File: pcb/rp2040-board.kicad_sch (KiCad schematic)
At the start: 61 parts, among them J1 DMX, J2 GPIO, J3 ELRS, J4 OLED, J5 SWD, J6 USB_C_Receptacle_USB2.0_16P, J7 AUDIO, SW1 TS-1187A-B-A-B, SW2 RotaryEncoder_Switch, SW3 TS-1187A-B-A-B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

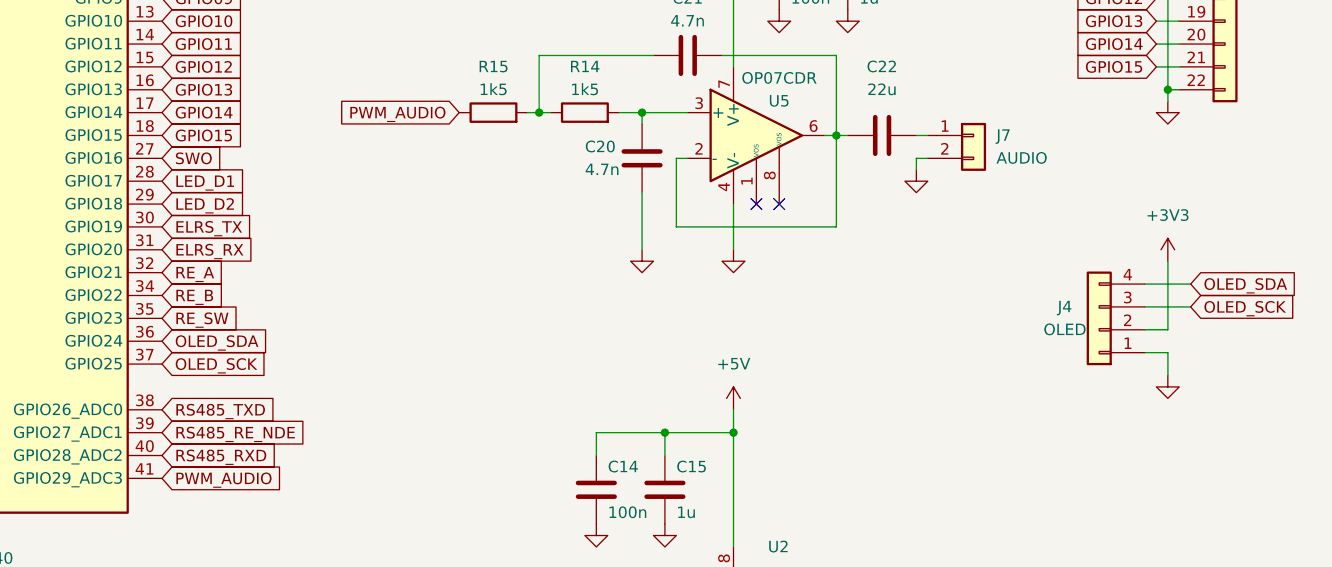
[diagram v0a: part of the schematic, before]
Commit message: fixed pin assignment issues
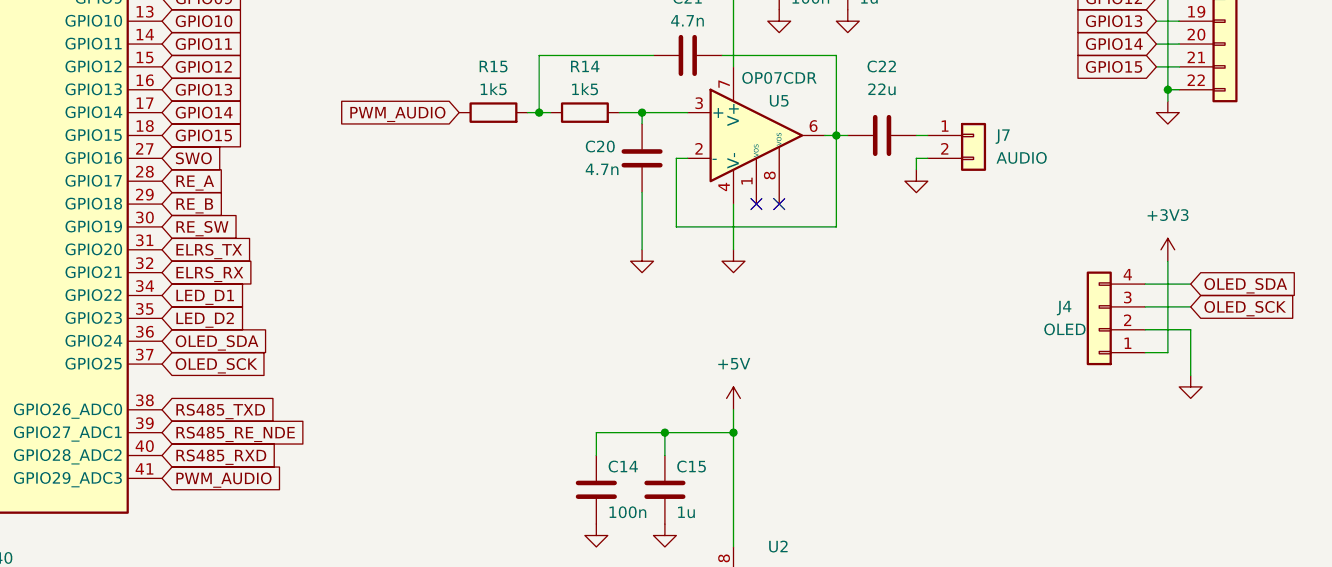
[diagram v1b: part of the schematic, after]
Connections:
- net +3V3: now also J4.1 (Pin_1); no longer J4.2 (Pin_2)
- net ELRS_RX: now also U3.32 (GPIO21); no longer U3.31 (GPIO20)
- net ELRS_TX: now also U3.31 (GPIO20); no longer U3.30 (GPIO19)
- net GND: now also J4.2 (Pin_2); no longer J4.1 (Pin_1)
- net LED_D1: now also U3.34 (GPIO22); no longer U3.28 (GPIO17)
- net LED_D2: now also U3.35 (GPIO23); no longer U3.29 (GPIO18)
- net RE_A: now also U3.28 (GPIO17); no longer U3.32 (GPIO21)
- net RE_B: now also U3.29 (GPIO18); no longer U3.34 (GPIO22)
- net RE_SW: now also U3.30 (GPIO19); no longer U3.35 (GPIO23)
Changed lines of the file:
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@@
   (no_connect (at 46.99 105.41))
   (no_connect (at 223.52 92.71))
+  (wire (pts (xy 266.7 109.22) (xy 264.16 109.22))
+    (stroke (width 0) (type default))
+  )
   (wire (pts (xy 106.68 181.61) (xy 105.41 181.61))
     (stroke (width 0) (type default))
@@
     (stroke (width 0) (type default))
   )
-  (wire (pts (xy 266.7 111.76) (xy 266.7 109.22))
-    (stroke (width 0) (type default))
-  )
   (wire (pts (xy 105.41 189.23) (xy 114.3 189.23))
     (stroke (width 0) (type default))
@@
     (stroke (width 0) (type default))
   )
+  (wire (pts (xy 269.24 106.68) (xy 269.24 111.76))
+    (stroke (width 0) (type default))
+  )
   (wire (pts (xy 49.53 162.56) (xy 50.8 162.56))
     (stroke (width 0) (type default))
@@
     (stroke (width 0) (type default))
   )
+  (wire (pts (xy 264.16 106.68) (xy 269.24 106.68))
+    (stroke (width 0) (type default))
+  )
   (wire (pts (xy 259.08 157.48) (xy 259.08 158.75))
     (stroke (width 0) (type default))
@@
     (stroke (width 0) (type default))
   )
-  (wire (pts (xy 264.16 106.68) (xy 266.7 106.68))
-    (stroke (width 0) (type default))
-  )
   (wire (pts (xy 265.43 54.61) (xy 267.97 54.61))
     (stroke (width 0) (type default))
@@
     (stroke (width 0) (type default))
   )
-  (wire (pts (xy 266.7 106.68) (xy 266.7 99.06))
+  (wire (pts (xy 266.7 99.06) (xy 266.7 109.22))
     (stroke (width 0) (type default))
   )
@@
   )
   (wire (pts (xy 64.77 27.94) (xy 72.39 27.94))
-    (stroke (width 0) (type default))
-  )
-  (wire (pts (xy 264.16 109.22) (xy 266.7 109.22))
     (stroke (width 0) (type default))
   )
@@
     )
   )
-  (global_label "RE_B" (shape input) (at 154.94 102.87 0) (fields_autoplaced)
-    (effects (font (size 1.27 1.27)) (justify left))
-    (property "Intersheetrefs" "${INTERSHEET_REFS}" (at 162.5818 102.87 0)
+  (global_label "RE_B" (shape input) (at 154.94 92.71 0) (fields_autoplaced)
+    (effects (font (size 1.27 1.27)) (justify left))
+    (property "Intersheetrefs" "${INTERSHEET_REFS}" (at 162.5818 92.71 0)
       (effects (font (size 1.27 1.27)) (justify left) hide)
     )
@@
     )
   )
-  (global_label "LED_D1" (shape input) (at 154.94 90.17 0) (fields_autoplaced)
-    (effects (font (size 1.27 1.27)) (justify left))
-    (property "Intersheetrefs" "${INTERSHEET_REFS}" (at 164.8194 90.17 0)
+  (global_label "LED_D1" (shape input) (at 154.94 102.87 0) (fields_autoplaced)
+    (effects (font (size 1.27 1.27)) (justify left))
+    (property "Intersheetrefs" "${INTERSHEET_REFS}" (at 164.8194 102.87 0)
       (effects (font (size 1.27 1.27)) (justify left) hide)
     )
@@
     )
   )
-  (global_label "ELRS_RX" (shape input) (at 154.94 97.79 0) (fields_autoplaced)
-    (effects (font (size 1.27 1.27)) (justify left))
-    (property "Intersheetrefs" "${INTERSHEET_REFS}" (at 166.0289 97.79 0)
+  (global_label "ELRS_RX" (shape input) (at 154.94 100.33 0) (fields_autoplaced)
+    (effects (font (size 1.27 1.27)) (justify left))
+    (property "Intersheetrefs" "${INTERSHEET_REFS}" (at 166.0289 100.33 0)
       (effects (font (size 1.27 1.27)) (justify left) hide)
     )
@@
     )
   )
-  (global_label "RE_SW" (shape input) (at 154.94 105.41 0) (fields_autoplaced)
-    (effects (font (size 1.27 1.27)) (justify left))
-    (property "Intersheetrefs" "${INTERSHEET_REFS}" (at 163.9727 105.41 0)
+  (global_label "RE_SW" (shape input) (at 154.94 95.25 0) (fields_autoplaced)
+    (effects (font (size 1.27 1.27)) (justify left))
+    (property "Intersheetrefs" "${INTERSHEET_REFS}" (at 163.9727 95.25 0)
       (effects (font (size 1.27 1.27)) (justify left) hide)
     )
@@
     )
   )
-  (global_label "ELRS_TX" (shape input) (at 154.94 95.25 0) (fields_autoplaced)
-    (effects (font (size 1.27 1.27)) (justify left))
-    (property "Intersheetrefs" "${INTERSHEET_REFS}" (at 165.7265 95.25 0)
+  (global_label "ELRS_TX" (shape input) (at 154.94 97.79 0) (fields_autoplaced)
+    (effects (font (size 1.27 1.27)) (justify left))
+    (property "Intersheetrefs" "${INTERSHEET_REFS}" (at 165.7265 97.79 0)
       (effects (font (size 1.27 1.27)) (justify left) hide)
     )
@@
     )
   )
-  (global_label "LED_D2" (shape input) (at 154.94 92.71 0) (fields_autoplaced)
-    (effects (font (size 1.27 1.27)) (justify left))
-    (property "Intersheetrefs" "${INTERSHEET_REFS}" (at 164.8194 92.71 0)
+  (global_label "LED_D2" (shape input) (at 154.94 105.41 0) (fields_autoplaced)
+    (effects (font (size 1.27 1.27)) (justify left))
+    (property "Intersheetrefs" "${INTERSHEET_REFS}" (at 164.8194 105.41 0)
       (effects (font (size 1.27 1.27)) (justify left) hide)
     )
@@
     )
   )
-  (global_label "RE_A" (shape input) (at 154.94 100.33 0) (fields_autoplaced)
-    (effects (font (size 1.27 1.27)) (justify left))
-    (property "Intersheetrefs" "${INTERSHEET_REFS}" (at 162.4004 100.33 0)
+  (global_label "RE_A" (shape input) (at 154.94 90.17 0) (fields_autoplaced)
+    (effects (font (size 1.27 1.27)) (justify left))
+    (property "Intersheetrefs" "${INTERSHEET_REFS}" (at 162.4004 90.17 0)
       (effects (font (size 1.27 1.27)) (justify left) hide)
     )
@@
     )
   )
-  (symbol (lib_id "power:GND") (at 266.7 111.76 0) (unit 1)
-    (in_bom yes) (on_board yes) (dnp no) (fields_autoplaced)
-    (property "Reference" "#PWR029" (at 266.7 118.11 0)
-      (effects (font (size 1.27 1.27)) hide)
-    )
-    (property "Value" "GND" (at 266.7 116.84 0)
-      (effects (font (size 1.27 1.27)) hide)
-    )
-    (property "Footprint" "" (at 266.7 111.76 0)
-      (effects (font (size 1.27 1.27)) hide)
-    )
-    (property "Datasheet" "" (at 266.7 111.76 0)
-      (effects (font (size 1.27 1.27)) hide)
-    )
+  (symbol (lib_id "power:GND") (at 269.24 111.76 0) (unit 1)
+    (in_bom yes) (on_board yes) (dnp no) (fields_autoplaced)
+    (property "Reference" "#PWR029" (at 269.24 118.11 0)
+      (effects (font (size 1.27 1.27)) hide)
+    )
+    (property "Value" "GND" (at 269.24 116.84 0)
+      (effects (font (size 1.27 1.27)) hide)
+    )
+    (property "Footprint" "" (at 269.24 111.76 0)
+      (effects (font (size 1.27 1.27)) hide)
+    )
+    (property "Datasheet" "" (at 269.24 111.76 0)
+      (effects (font (size 1.27 1.27)) hide)
+    )

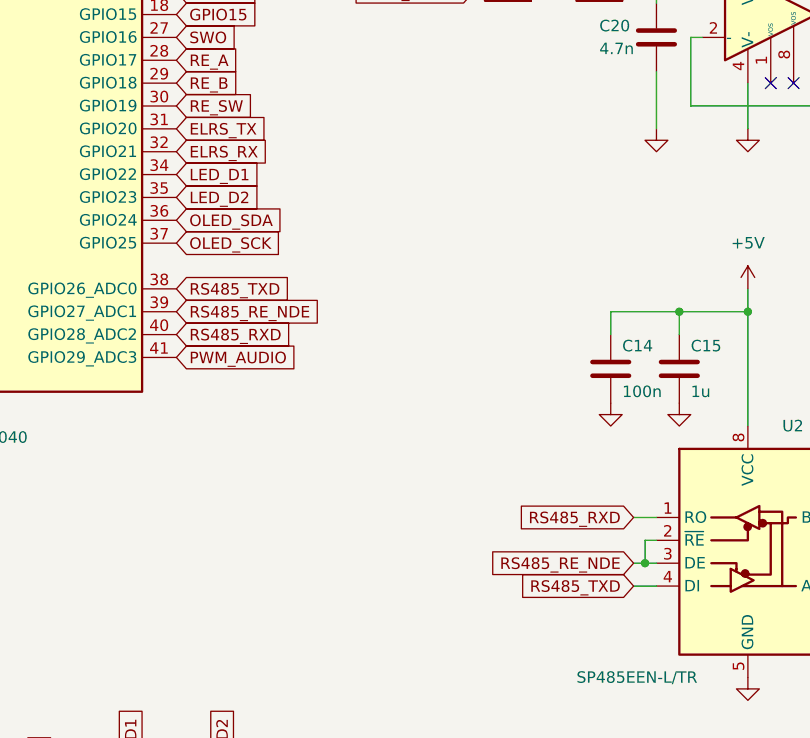
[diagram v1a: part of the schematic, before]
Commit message: pin assignment issues fixed
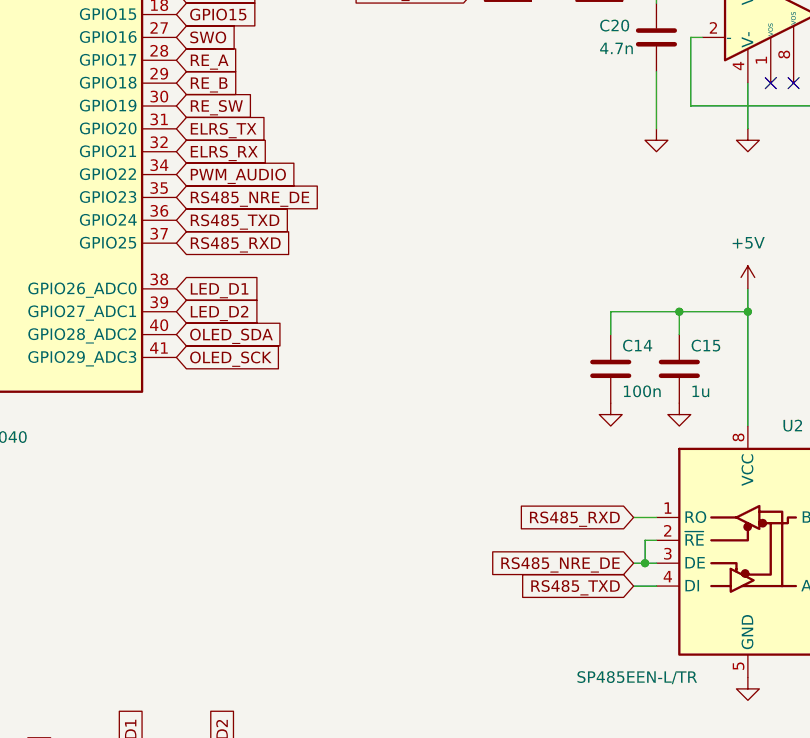
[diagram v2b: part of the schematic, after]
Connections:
- net LED_D1: now also U3.38 (GPIO26_ADC0); no longer U3.34 (GPIO22)
- net LED_D2: now also U3.39 (GPIO27_ADC1); no longer U3.35 (GPIO23)
- net OLED_SCK: now also U3.41 (GPIO29_ADC3); no longer U3.37 (GPIO25)
- net OLED_SDA: now also U3.40 (GPIO28_ADC2); no longer U3.36 (GPIO24)
- net PWM_AUDIO: now also U3.34 (GPIO22); no longer U3.41 (GPIO29_ADC3)
- net RS485_RXD: now also U3.37 (GPIO25); no longer U3.40 (GPIO28_ADC2)
- net RS485_TXD: now also U3.36 (GPIO24); no longer U3.38 (GPIO26_ADC0)
- net RS485_RE_NDE renamed RS485_NRE_DE
- net RS485_NRE_DE: now also U3.35 (GPIO23); no longer U3.39 (GPIO27_ADC1)
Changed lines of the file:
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@@
     )
   )
-  (global_label "RS485_TXD" (shape input) (at 154.94 115.57 0) (fields_autoplaced)
-    (effects (font (size 1.27 1.27)) (justify left))
-    (property "Intersheetrefs" "${INTERSHEET_REFS}" (at 168.4479 115.57 0)
+  (global_label "RS485_TXD" (shape input) (at 154.94 107.95 0) (fields_autoplaced)
+    (effects (font (size 1.27 1.27)) (justify left))
+    (property "Intersheetrefs" "${INTERSHEET_REFS}" (at 168.4479 107.95 0)
       (effects (font (size 1.27 1.27)) (justify left) hide)
     )
@@
     )
   )
-  (global_label "RS485_RXD" (shape input) (at 154.94 120.65 0) (fields_autoplaced)
-    (effects (font (size 1.27 1.27)) (justify left))
-    (property "Intersheetrefs" "${INTERSHEET_REFS}" (at 168.7503 120.65 0)
+  (global_label "RS485_RXD" (shape input) (at 154.94 110.49 0) (fields_autoplaced)
+    (effects (font (size 1.27 1.27)) (justify left))
+    (property "Intersheetrefs" "${INTERSHEET_REFS}" (at 168.7503 110.49 0)
       (effects (font (size 1.27 1.27)) (justify left) hide)
     )
@@
     )
   )
-  (global_label "LED_D1" (shape input) (at 154.94 102.87 0) (fields_autoplaced)
-    (effects (font (size 1.27 1.27)) (justify left))
-    (property "Intersheetrefs" "${INTERSHEET_REFS}" (at 164.8194 102.87 0)
+  (global_label "LED_D1" (shape input) (at 154.94 115.57 0) (fields_autoplaced)
+    (effects (font (size 1.27 1.27)) (justify left))
+    (property "Intersheetrefs" "${INTERSHEET_REFS}" (at 164.8194 115.57 0)
       (effects (font (size 1.27 1.27)) (justify left) hide)
     )
@@
     )
   )
-  (global_label "PWM_AUDIO" (shape input) (at 154.94 123.19 0) (fields_autoplaced)
-    (effects (font (size 1.27 1.27)) (justify left))
-    (property "Intersheetrefs" "${INTERSHEET_REFS}" (at 168.69 123.19 0)
+  (global_label "PWM_AUDIO" (shape input) (at 154.94 102.87 0) (fields_autoplaced)
+    (effects (font (size 1.27 1.27)) (justify left))
+    (property "Intersheetrefs" "${INTERSHEET_REFS}" (at 168.69 102.87 0)
       (effects (font (size 1.27 1.27)) (justify left) hide)
     )
@@
     )
   )
-  (global_label "RS485_RE_NDE" (shape input) (at 154.94 118.11 0) (fields_autoplaced)
-    (effects (font (size 1.27 1.27)) (justify left))
-    (property "Intersheetrefs" "${INTERSHEET_REFS}" (at 172.1369 118.11 0)
+  (global_label "RS485_NRE_DE" (shape input) (at 154.94 105.41 0) (fields_autoplaced)
+    (effects (font (size 1.27 1.27)) (justify left))
+    (property "Intersheetrefs" "${INTERSHEET_REFS}" (at 172.1369 105.41 0)
       (effects (font (size 1.27 1.27)) (justify left) hide)
     )
@@
     )
   )
-  (global_label "OLED_SDA" (shape input) (at 154.94 107.95 0) (fields_autoplaced)
-    (effects (font (size 1.27 1.27)) (justify left))
-    (property "Intersheetrefs" "${INTERSHEET_REFS}" (at 167.2385 107.95 0)
+  (global_label "OLED_SDA" (shape input) (at 154.94 120.65 0) (fields_autoplaced)
+    (effects (font (size 1.27 1.27)) (justify left))
+    (property "Intersheetrefs" "${INTERSHEET_REFS}" (at 167.2385 120.65 0)
       (effects (font (size 1.27 1.27)) (justify left) hide)
     )
@@
     )
   )
-  (global_label "OLED_SCK" (shape input) (at 154.94 110.49 0) (fields_autoplaced)
-    (effects (font (size 1.27 1.27)) (justify left))
-    (property "Intersheetrefs" "${INTERSHEET_REFS}" (at 167.4199 110.49 0)
+  (global_label "OLED_SCK" (shape input) (at 154.94 123.19 0) (fields_autoplaced)
+    (effects (font (size 1.27 1.27)) (justify left))
+    (property "Intersheetrefs" "${INTERSHEET_REFS}" (at 167.4199 123.19 0)
       (effects (font (size 1.27 1.27)) (justify left) hide)
     )
@@
     )
   )
-  (global_label "LED_D2" (shape input) (at 154.94 105.41 0) (fields_autoplaced)
-    (effects (font (size 1.27 1.27)) (justify left))
-    (property "Intersheetrefs" "${INTERSHEET_REFS}" (at 164.8194 105.41 0)
+  (global_label "LED_D2" (shape input) (at 154.94 118.11 0) (fields_autoplaced)
+    (effects (font (size 1.27 1.27)) (justify left))
+    (property "Intersheetrefs" "${INTERSHEET_REFS}" (at 164.8194 118.11 0)
       (effects (font (size 1.27 1.27)) (justify left) hide)
     )
@@
     )
   )
-  (global_label "RS485_RE_NDE" (shape input) (at 205.74 146.05 180) (fields_autoplaced)
+  (global_label "RS485_NRE_DE" (shape input) (at 205.74 146.05 180) (fields_autoplaced)
     (effects (font (size 1.27 1.27)) (justify right))
     (property "Intersheetrefs" "${INTERSHEET_REFS}" (at 188.5431 146.05 0)

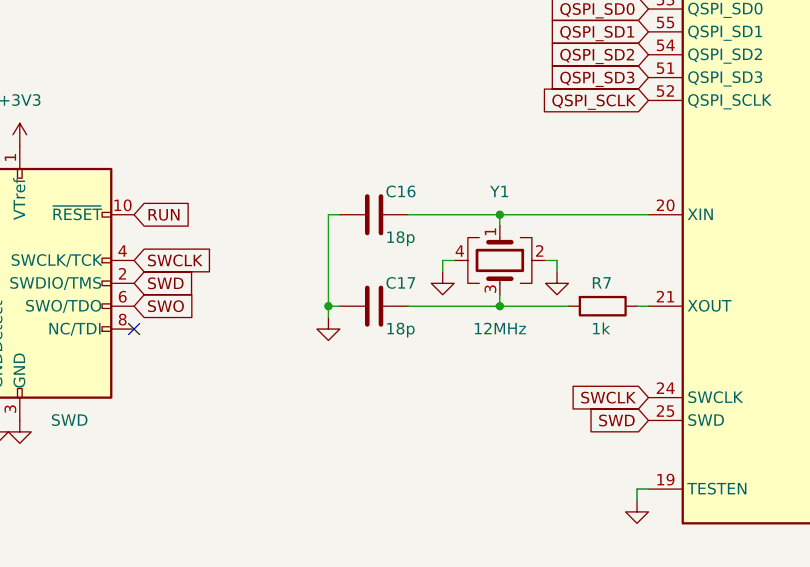
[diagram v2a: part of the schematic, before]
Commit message: xtal capacitance closer to the target
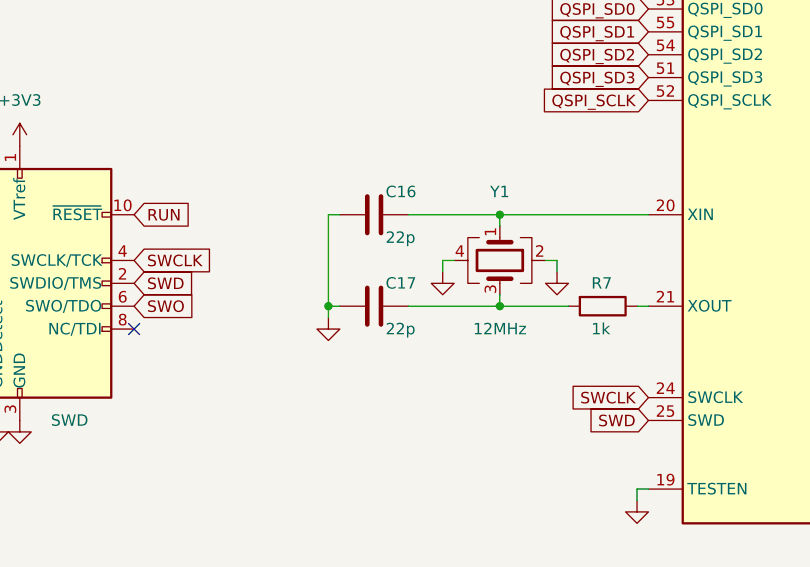
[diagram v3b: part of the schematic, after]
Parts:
- C16, C17: value 18p -> 22p; LCSC Part C1549 -> C1555
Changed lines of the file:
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@@
       (effects (font (size 1.27 1.27)) (justify left))
     )
-    (property "Value" "18p" (at 74.93 105.41 90)
+    (property "Value" "22p" (at 74.93 105.41 90)
       (effects (font (size 1.27 1.27)) (justify left))
     )
@@
       (effects (font (size 1.27 1.27)) hide)
     )
-    (property "LCSC Part" "C1549" (at 73.66 102.87 0)
+    (property "LCSC Part" "C1555" (at 73.66 102.87 0)
       (effects (font (size 1.27 1.27)) hide)
     )
@@
       (effects (font (size 1.27 1.27)) (justify left))
     )
-    (property "Value" "18p" (at 74.93 95.25 90)
+    (property "Value" "22p" (at 74.93 95.25 90)
       (effects (font (size 1.27 1.27)) (justify left))
     )
@@
       (effects (font (size 1.27 1.27)) hide)
     )
-    (property "LCSC Part" "C1549" (at 73.66 92.71 0)
-      (effects (font (size 1.27 1.27)) hide)
-    )
+    (property "LCSC Part" "C1555" (at 73.66 92.71 0)
+      (effects (font (size 1.27 1.27)) hide)
+    )

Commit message: WIP on the second PCB, also resaved with kicad 9
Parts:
- removed C24: 1u, Capacitor_SMD:C_0402_1005Metric, symbol Device:C
- removed J7: AUDIO, Connector_PinHeader_2.54mm:PinHeader_1x02_P2.54mm_Vertical, symbol Connector_Generic:Conn_01x02
- removed R14, R15: 1k5, Resistor_SMD:R_0402_1005Metric, symbol Device:R
- removed R16: 0, Resistor_SMD:R_0603_1608Metric, symbol Device:R
- removed U5: OP07CDR, Package_SO:SOIC-8_3.9x4.9mm_P1.27mm, symbol Amplifier_Operational:OP07
- added U5, U6: DRV8837, Package_SON:WSON-8-1EP_2x2mm_P0.5mm_EP0.9x1.6mm, symbol Driver_Motor:DRV8837
- C20, C21: value 4.7n -> 100n; LCSC Part C1538 -> C1525
- C22: value 22u -> 100n; footprint Capacitor_SMD:C_0805_2012Metric -> Capacitor_SMD:C_0402_1005Metric; LCSC Part C45783 -> C1525
- U1: footprint Package_SO:SOIC-8_5.23x5.23mm_P1.27mm -> Package_SON:WSON-8-1EP_6x5mm_P1.27mm_EP3.4x4.3mm; symbol Memory_Flash:W25Q128JVS -> Memory_Flash:W25Q32JVZP; LCSC Part C97521 -> C571260
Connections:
- net +3V3: now also C20.2, C22.2, U5.8 (VCC), U6.8 (VCC)
- net GND: now also C20.1, C21.2, C22.1, U1.9 (EP), U5.4 (GND), U5.9 (GND), U6.4 (GND), U6.9 (GND); no longer C20.2
- net +6V: now reaches C21.1
- net +6V: now also C23.1, U5.1 (VM), U6.1 (VM)
- net PWM_AUDIO: no longer names the net of U3.34 (GPIO22)
- new net DRVIN1A: U5.6 (IN1)
- new net DRVIN1B: U5.5 (IN2)
- new net DRVIN2A: U6.6 (IN1)
- new net DRVIN2B: U6.5 (IN2)
- new net DRVNSLEEP: U5.7 (~{SLEEP}), U6.7 (~{SLEEP})
- new net DRVOUT1A: U5.2 (OUT1)
- new net DRVOUT1B: U5.3 (OUT2)
- new net DRVOUT2A: U6.2 (OUT1)
- new net DRVOUT2B: U6.3 (OUT2)
- no-connect marks 7 -> 5
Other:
- moved on the sheet: J2, J3, J4, J5
